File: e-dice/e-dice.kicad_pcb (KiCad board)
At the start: 2 copper layers, 105.5 x 34.5 mm, 74 parts, among them J1 mid_conn_1, J2 top_conn_1, J3 mid_conn_2, J4 top_conn_2, J6 bot_conn_1, J7 bot_conn_2, J8 mid_conn_3, J9 mid_conn_4, Q1 2N3904, Q2 2N3904, Q3 2N3904, Q4 2N3906, Q5 2N3904, Q6 2N3904, Q7 2N3904, SW1 SW_SPDT, U1 4017

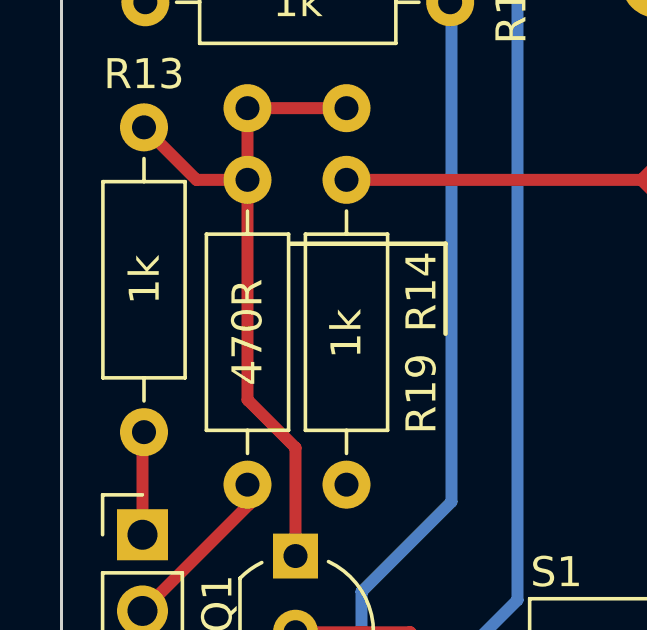
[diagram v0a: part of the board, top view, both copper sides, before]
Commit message: Finished crossing for production, modified other
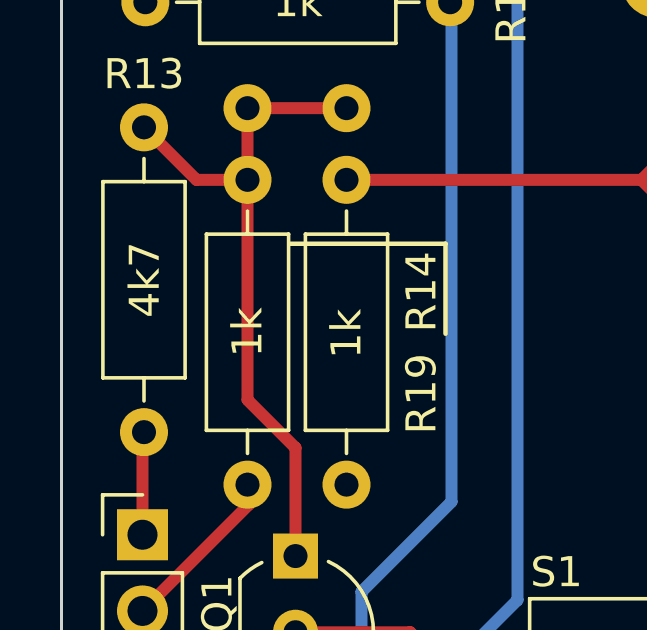
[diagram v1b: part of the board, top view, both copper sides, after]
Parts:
- R11, R14: value 470R -> 1k
- R12, R13: value 1k -> 4k7
